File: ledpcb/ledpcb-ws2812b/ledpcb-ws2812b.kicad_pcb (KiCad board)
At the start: 2 copper layers, 18 x 220 mm, 29 parts, among them J1 JST_XA_B04B, J2 JST_XA_B03B, J3 JST_XA_B03B

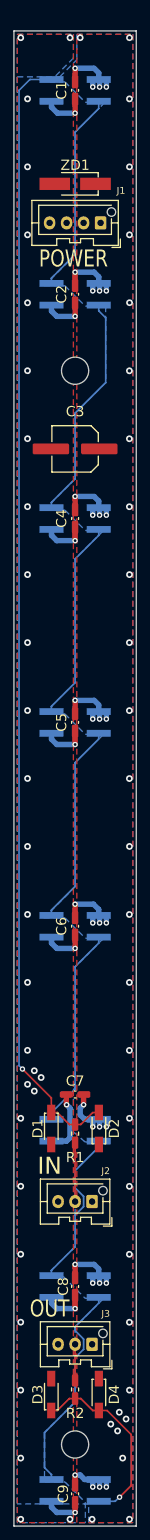
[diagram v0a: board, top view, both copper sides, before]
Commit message: Changes for ordering with JLCPCB.
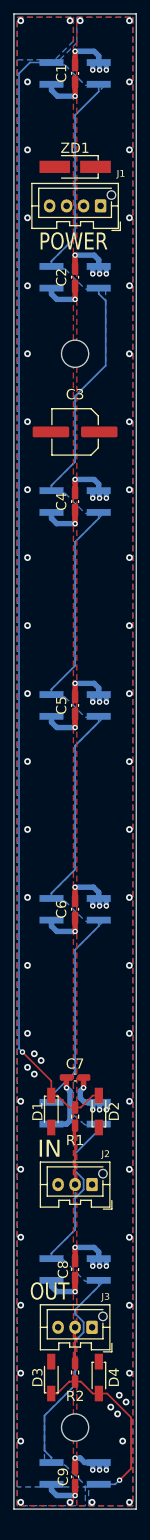
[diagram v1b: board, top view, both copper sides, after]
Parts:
- moved C1 2.50 mm to (112.0, -1.25)
- moved C2 2.50 mm to (112.0, 28.8)
- moved C3 2.50 mm to (112.0, 51.5)
- moved C4 2.50 mm to (112.0, 61.8)
- moved C5 2.50 mm to (112.0, 91.8)
- moved C6 2.50 mm to (112.0, 121.8)
- moved C7 2.50 mm to (112.0, 146.5)
- moved C8 2.50 mm to (112.0, 174.8)
- moved C9 2.50 mm to (112.0, 205.2)
- moved D1 2.50 mm to (108.5, 151.5)
- moved D2 2.50 mm to (115.5, 151.5)
- moved D3 2.50 mm to (108.5, 190.7)
- moved D4 2.50 mm to (115.5, 190.7)
- moved H1 2.50 mm to (112.0, 40.0)
- moved H2 2.50 mm to (112.0, 198.0)
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
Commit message: Merge some changes between desktop and laptop manually...
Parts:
- added REF**: JLCPCB PCBA tooling hole, ledpcb:JLCPCB PCBA tooling hole, F.Cu at (104.2, 208.8)
- added REF**: JLCPCB PCBA tooling hole, ledpcb:JLCPCB PCBA tooling hole, F.Cu at (119.8, -8.75)
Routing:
- net GND: vias 37 -> 36
- net +5V: vias 61 -> 60
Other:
- board text added: "JLCJLCJLCJLC"
- board text added: "WACCA aftermarket LED PCB replacement - using WS2812b's Failure conditions: two connected LEDs broken, or final LED broken."
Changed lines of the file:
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@@
     )
+  )
+  (footprint "ledpcb:JLCPCB PCBA tooling hole" (layer "F.Cu")
+    (at 104.25 208.75)
+    (attr through_hole board_only exclude_from_pos_files exclude_from_bom)
+    (fp_text reference "REF**" (at 0 -2.2 unlocked) (layer "F.SilkS") hide
+      (effects (font (size 1 1) (thickness 0.15)))
+    )
+    (fp_text value "JLCPCB PCBA tooling hole" (at 0 2.1 unlocked) (layer "F.Fab")
+      (effects (font (size 1 1) (thickness 0.15)))
+    )
+    (fp_text user "${REFERENCE}" (at 0 -2 unlocked) (layer "F.Fab")
+      (effects (font (size 1 1) (thickness 0.15)))
+    )
+    (pad "" np_thru_hole circle (at 0 0) (size 1.152 1.152) (drill 1.152) (layers F&B.Cu *.Mask)
+      (solder_mask_margin 0.074))
   )
   (footprint "ledpcb:R_0603_1608Metric" (layer "F.Cu")
@@
     )
   )
+  (footprint "ledpcb:JLCPCB PCBA tooling hole" (layer "F.Cu")
+    (at 119.75 -8.75)
+    (attr through_hole board_only exclude_from_pos_files exclude_from_bom)
+    (fp_text reference "REF**" (at 0 -2.2 unlocked) (layer "F.SilkS") hide
+      (effects (font (size 1 1) (thickness 0.15)))
+    )
+    (fp_text value "JLCPCB PCBA tooling hole" (at 0 2.1 unlocked) (layer "F.Fab")
+      (effects (font (size 1 1) (thickness 0.15)))
+    )
+    (fp_text user "${REFERENCE}" (at 0 -2 unlocked) (layer "F.Fab")
+      (effects (font (size 1 1) (thickness 0.15)))
+    )
+    (pad "" np_thru_hole circle (at 0 0) (size 1.152 1.152) (drill 1.152) (layers F&B.Cu *.Mask)
+      (solder_mask_margin 0.074))
+  )
   (footprint "ledpcb:LED_WS2812B_PLCC4_5.0x5.0mm_P3.2mm" (layer "B.Cu")
     (at 112 28.75)
@@
     (effects (font (size 2.5 2) (thickness 0.3)))
   )
+  (gr_text "JLCJLCJLCJLC" (at 112 -6.25) (layer "F.SilkS")
+    (effects (font (size 1.5 1.5) (thickness 0.2)))
+  )
+  (gr_text "WACCA aftermarket LED PCB replacement - using WS2812b's\n\n\n\n\nFailure conditions: two connected LEDs broken, or final LED broken." (at 112 102.75 90) (layer "F.SilkS")
+    (effects (font (size 1.5 1.5) (thickness 0.3)))
+  )
   (dimension (type aligned) (layer "Dwgs.User")
     (pts (xy 112 -10) (xy 112 40))
     (height -12.25)
-    (gr_text "50,0000 mm" (at 123.1 15 90) (layer "Dwgs.User")
+    (gr_text "50.0000 mm" (at 123.1 15 90) (layer "Dwgs.User")
       (effects (font (size 1 1) (thickness 0.15)))
     )
@@
     (pts (xy 122 15) (xy 122 40))
     (height -6.5)
-    (gr_text "25,0000 mm" (at 127.35 27.5 90) (layer "Dwgs.User")
+    (gr_text "25.0000 mm" (at 127.35 27.5 90) (layer "Dwgs.User")
       (effects (font (size 1 1) (thickness 0.15)))
     )
@@
     (pts (xy 122 159) (xy 122 180))
     (height -6.5)
-    (gr_text "21,0000 mm" (at 127.35 169.5 90) (layer "Dwgs.User")
+    (gr_text "21.0000 mm" (at 127.35 169.5 90) (layer "Dwgs.User")
       (effects (font (size 1 1) (thickness 0.15)))
     )
@@
     (pts (xy 122 180) (xy 122 210))
     (height -6.5)
-    (gr_text "30,0000 mm" (at 127.35 195 90) (layer "Dwgs.User")
+    (gr_text "30.0000 mm" (at 127.35 195 90) (layer "Dwgs.User")
       (effects (font (size 1 1) (thickness 0.15)))
     )
@@
     (pts (xy 112 151.75) (xy 112 174.75))
     (height 13)
-    (gr_text "23,0000 mm" (at 97.85 163.25 90) (layer "Dwgs.User")
+    (gr_text "23.0000 mm" (at 97.85 163.25 90) (layer "Dwgs.User")
       (effects (font (size 1 1) (thickness 0.15)))
     )
@@
     (pts (xy 112 204.75) (xy 112 174.75))
     (height -13)
-    (gr_text "30,0000 mm" (at 97.85 189.75 90) (layer "Dwgs.User")
+    (gr_text "30.0000 mm" (at 97.85 189.75 90) (layer "Dwgs.User")
       (effects (font (size 1 1) (thickness 0.15)))
     )
@@
     (pts (xy 122 -10) (xy 122 210))
     (height -10)
-    (gr_text "220,0000 mm" (at 130.85 100 90) (layer "Dwgs.User")
+    (gr_text "220.0000 mm" (at 130.85 100 90) (layer "Dwgs.User")
       (effects (font (size 1 1) (thickness 0.15)))
     )
@@
     (pts (xy 112 91.75) (xy 112 61.75))
     (height -13)
-    (gr_text "30,0000 mm" (at 97.85 76.75 90) (layer "Dwgs.User")
+    (gr_text "30.0000 mm" (at 97.85 76.75 90) (layer "Dwgs.User")
       (effects (font (size 1 1) (thickness 0.15)))
     )
@@
     (pts (xy 122 -10) (xy 122 15))
     (height -6.5)
-    (gr_text "25,0000 mm" (at 127.35 2.5 90) (layer "Dwgs.User")
+    (gr_text "25.0000 mm" (at 127.35 2.5 90) (layer "Dwgs.User")
       (effects (font (size 1 1) (thickness 0.15)))
     )
@@
     (pts (xy 121 -10) (xy 103 -10))
     (height 5.099999)
-    (gr_text "18,0000 mm" (at 112 -16.249999) (layer "Dwgs.User")
+    (gr_text "18.0000 mm" (at 112 -16.249999) (layer "Dwgs.User")
       (effects (font (size 1 1) (thickness 0.15)))
     )
@@
     (pts (xy 112 28.75) (xy 112 -1.25))
     (height -13)
-    (gr_text "30,0000 mm" (at 97.85 13.75 90) (layer "Dwgs.User")
+    (gr_text "30.0000 mm" (at 97.85 13.75 90) (layer "Dwgs.User")
       (effects (font (size 1 1) (thickness 0.15)))
     )
@@
     (pts (xy 112 61.75) (xy 112 28.75))
     (height -13)
-    (gr_text "33,0000 mm" (at 97.85 45.25 90) (layer "Dwgs.User")
+    (gr_text "33.0000 mm" (at 97.85 45.25 90) (layer "Dwgs.User")
       (effects (font (size 1 1) (thickness 0.15)))
     )
@@
     (pts (xy 112 210) (xy 112 198))
     (height 12.25)
-    (gr_text "12,0000 mm" (at 123.1 204 90) (layer "Dwgs.User")
+    (gr_text "12.0000 mm" (at 123.1 204 90) (layer "Dwgs.User")
       (effects (font (size 1 1) (thickness 0.15)))
     )
@@
     (pts (xy 112 151.75) (xy 112 121.75))
     (height -13)
-    (gr_text "30,0000 mm" (at 97.85 136.75 90) (layer "Dwgs.User")
+    (gr_text "30.0000 mm" (at 97.85 136.75 90) (layer "Dwgs.User")
       (effects (font (size 1 1) (thickness 0.15)))
     )
@@
     (pts (xy 112 210) (xy 112 204.75))
     (height -13)
-    (gr_text "5,2500 mm" (at 97.85 207.375 90) (layer "Dwgs.User")
+    (gr_text "5.2500 mm" (at 97.85 207.375 90) (layer "Dwgs.User")
       (effects (font (size 1 1) (thickness 0.15)))
     )
@@
     (pts (xy 122 40) (xy 122 159))
     (height -6.5)
-    (gr_text "119,0000 mm" (at 127.35 99.5 90) (layer "Dwgs.User")
+    (gr_text "119.0000 mm" (at 127.35 99.5 90) (layer "Dwgs.User")
       (effects (font (size 1 1) (thickness 0.15)))
     )
@@
     (pts (xy 112 -1.25) (xy 112 -10))
     (height -13)
-    (gr_text "8,7500 mm" (at 97.85 -5.625 90) (layer "Dwgs.User")
+    (gr_text "8.7500 mm" (at 97.85 -5.625 90) (layer "Dwgs.User")
       (effects (font (size 1 1) (thickness 0.15)))
     )
@@
     (pts (xy 112 40) (xy 112 198))
     (height -12.25)
-    (gr_text "158,0000 mm" (at 123.1 119 90) (layer "Dwgs.User")
+    (gr_text "158.0000 mm" (at 123.1 119 90) (layer "Dwgs.User")
       (effects (font (size 1 1) (thickness 0.15)))
     )
@@
     (pts (xy 112 121.75) (xy 112 91.75))
     (height -13)
-    (gr_text "30,0000 mm" (at 97.85 106.75 90) (layer "Dwgs.User")
+    (gr_text "30.0000 mm" (at 97.85 106.75 90) (layer "Dwgs.User")
       (effects (font (size 1 1) (thickness 0.15)))
     )
@@
   (via (at 116.6 174.25) (size 0.8) (drill 0.4) (layers "F.Cu" "B.Cu") (net 1))
   (via (at 119.987809 160.009942) (size 1) (drill 0.5) (layers "F.Cu" "B.Cu") (free) (net 1))
-  (via (at 120 -9) (size 1) (drill 0.5) (layers "F.Cu" "B.Cu") (free) (net 1))
   (via (at 112 202.5) (size 0.8) (drill 0.4) (layers "F.Cu" "B.Cu") (net 1))
   (via (at 115.6 28.25) (size 0.8) (drill 0.4) (layers "F.Cu" "B.Cu") (net 1))
@@
   (via (at 106 143) (size 1) (drill 0.5) (layers "F.Cu" "B.Cu") (free) (net 2))
   (via (at 112 125) (size 0.8) (drill 0.4) (layers "F.Cu" "B.Cu") (net 2))
-  (via (at 104 209) (size 1) (drill 0.5) (layers "F.Cu" "B.Cu") (free) (net 2))
   (via (at 105 90) (size 1) (drill 0.5) (layers "F.Cu" "B.Cu") (free) (net 2))
   (via (at 105 10) (size 1) (drill 0.5) (layers "F.Cu" "B.Cu") (free) (net 2))
